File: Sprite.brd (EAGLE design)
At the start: 35 x 44.6 mm, 24 parts, among them P1 SPRITE_PIN, P2 SPRITE_PIN, U1 CC430F5137, X1 TCXO_7Z

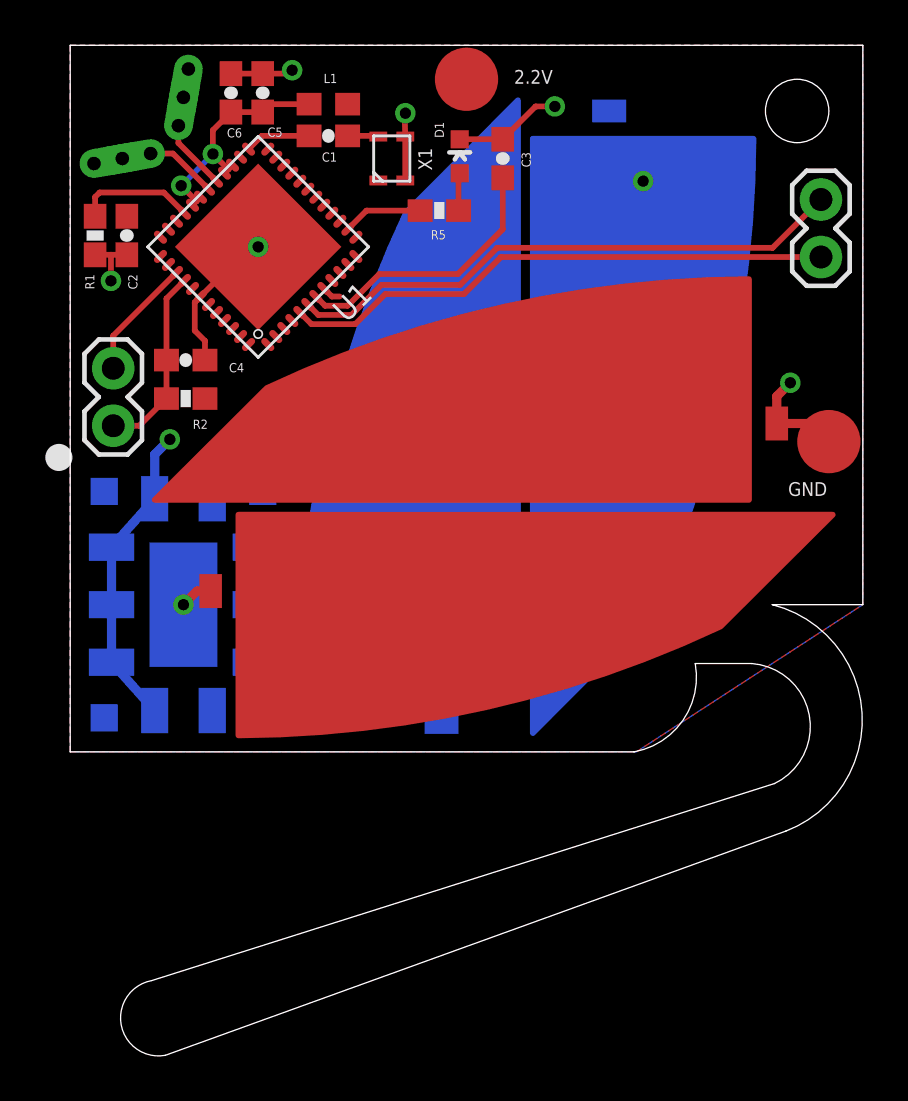
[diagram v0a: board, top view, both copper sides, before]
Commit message: Added murata UMAC battery
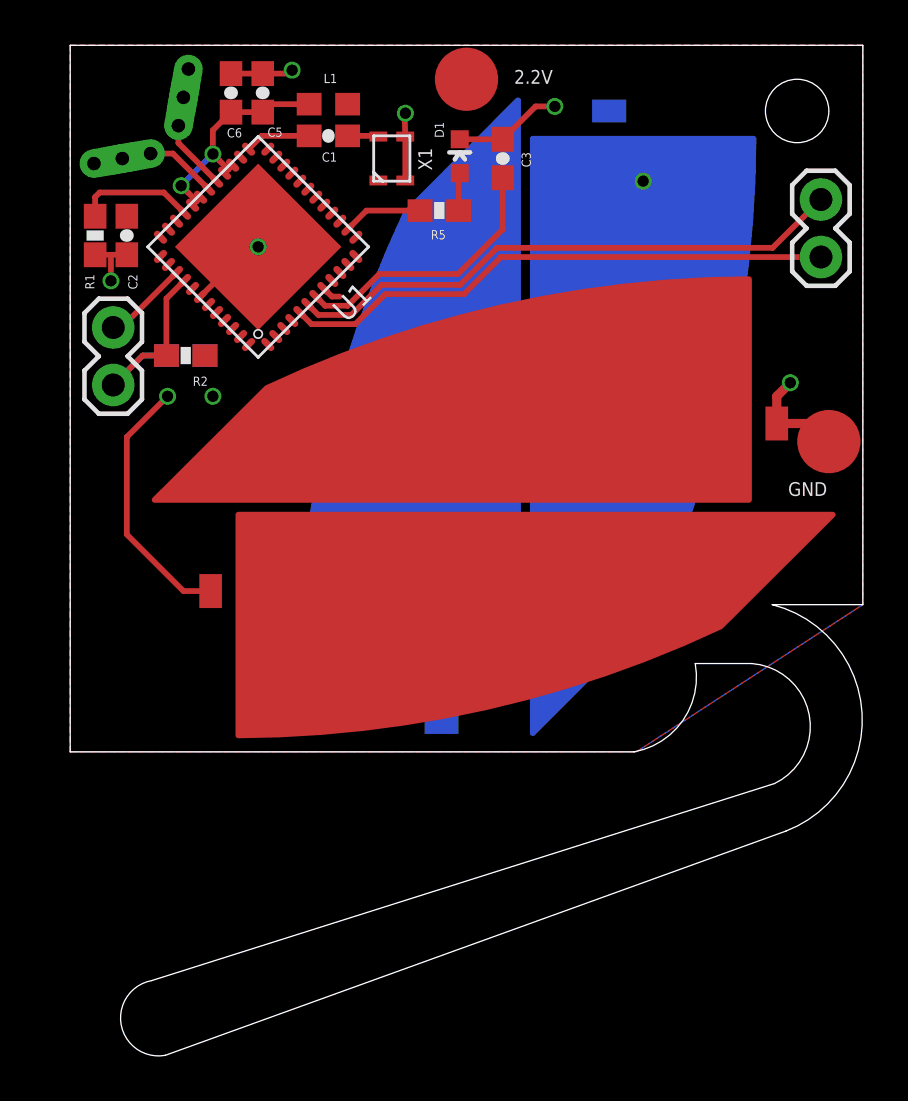
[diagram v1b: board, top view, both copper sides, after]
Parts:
- U$1: value FASTCAP -> UMAC; device FastCap:FASTCAP -> UMAC:UMAC
- moved U$1 6.71 mm to (5.30, 17.0), turned to 90 degrees
- moved R2 1.90 mm to (5.10, 21.3)
- moved JP2 1.80 mm to (1.90, 20.0)
- moved C4 0.20 mm to (5.10, 21.3), flipped to the bottom, turned to 0 degrees
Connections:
- net GND: now also U$1.V-; no longer U$1.P11, U$1.P5, U$1.P6, U$1.P7, U$1.P8, U$1.P9
- net VCC: now also U$1.V+; no longer U$1.P1, U$1.P10, U$1.P2, U$1.P3, U$1.P4
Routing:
- net VCC: track 37.8 -> 24.1 mm, vias 2 -> 1
- net GND: track 25.9 -> 33.0 mm, vias 7 -> 6
- net TEST: track 5.39 -> 3.83 mm
- net RST: track 8.39 -> 9.42 mm
